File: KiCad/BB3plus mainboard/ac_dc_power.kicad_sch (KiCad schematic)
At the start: 96 parts, among them IC7 SN74HCS02PWR, IC8 TPS62933ODRLR, IC9 LM64460CPPQRYFRQ1, K1 AZ943-1CH-12DE, K2 AZ943-1CH-12DE, Q3 2N7002, Q4 2N7002, Q5 MMBT5401, Q6 DMP3013SFV-7, SW1 WBL2UOAGQR05CLR, X10 B3P-VH-FB-B, X11 B3P-VH-FB-B, X5 571-0400, X6 GSP1.9101.1, X7 1-726388-2, X8 B3P-VH-FB-B, X9 B3P-VH-FB-B

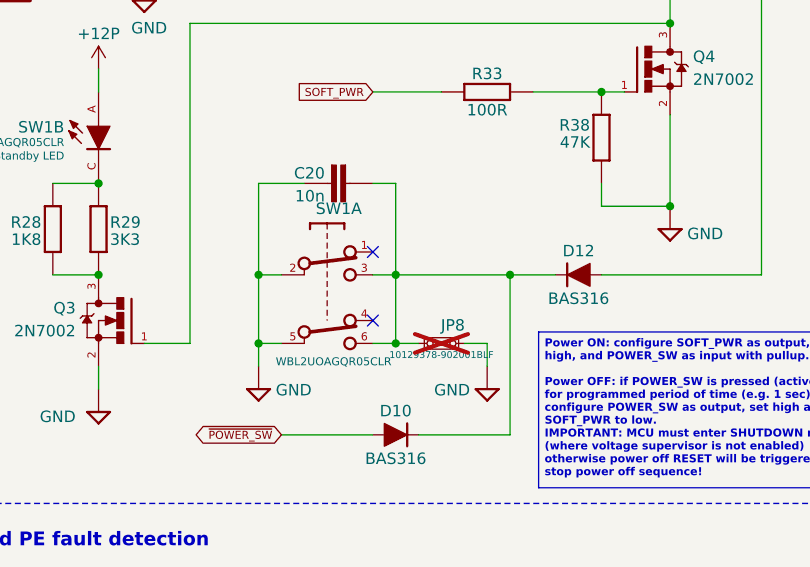
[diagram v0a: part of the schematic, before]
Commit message: JP8 added as mandatory
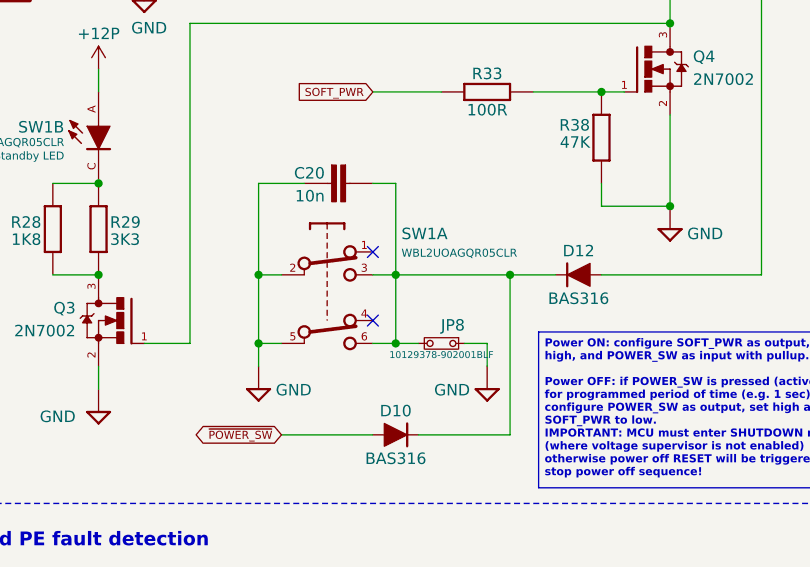
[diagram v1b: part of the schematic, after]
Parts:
- JP8: now fitted; now in the parts list
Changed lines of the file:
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@@
 	(title_block
 		(title "${project_name}")
-		(date "2026-10-05")
+		(date "2026-10-06")
 		(rev "${project_version}")
 		(company "${project_creator}")
@@
 		(dnp no)
 		(property "Reference" "SW1"
-			(at 77.47 117.856 0)
+			(at 86.995 120.65 0)
 			(show_name no)
 			(do_not_autoplace yes)
@@
 		)
 		(property "Value" "WBL2UOAGQR05CLR"
-			(at 73.025 134.62 0)
+			(at 86.995 122.555 0)
 			(show_name no)
 			(do_not_autoplace yes)
@@
 		(body_style 1)
 		(exclude_from_sim no)
-		(in_bom no)
+		(in_bom yes)
 		(on_board yes)
-		(in_pos_files no)
-		(dnp yes)
+		(in_pos_files yes)
+		(dnp no)
 		(property "Reference" "JP8"
 			(at 92.71 130.81 0)

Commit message: #22
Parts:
- renumbered JP8 to JP9
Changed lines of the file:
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@@
 	(title_block
 		(title "${project_name}")
-		(date "2026-10-06")
+		(date "2026-10-08")
 		(rev "${project_version}")
 		(company "${project_creator}")
@@
 		(in_pos_files yes)
 		(dnp no)
-		(property "Reference" "JP8"
-			(at 92.71 130.81 0)
+		(property "Reference" "JP9"
+			(at 91.44 130.81 0)
 			(show_name no)
 			(do_not_autoplace no)
@@
 			(project "BB3plus mainboard"
 				(path "/1df84e4f-233a-4f72-9418-c0020706bb76/451f238c-56e9-49de-804a-2a19deb9fc4a"
-					(reference "JP8")
+					(reference "JP9")
 					(unit 1)
 				)

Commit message: PE fault detection section updated
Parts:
- added C27: 100n, PCM_EEZ_passives:C_0603_1608Metric, symbol PCM_EEZ_passives:C-EU
- added JP10: 10129378-904001BLF, PCM_EEZ_connectors:PinHeader_1x04_P2.54mm_vert_numbered, symbol PCM_EEZ_unsorted:JP4 open 2.54mm THT
- R31, R32: value 33K/0.5W -> 100K/0.5W; footprint PCM_EEZ_passives:R_0805_2012Metric -> PCM_EEZ_passives:R_1210_3225Metric; DigiKey 10-ERJ-P06F3302VCT-ND -> 13-RC2010JK-07100KLCT-ND; LCSC C441988 -> C606205; Mouser 667-ERJ-P06F3302V -> 603-RC2010JK-07100KL; TME ERJP06F3302V -> CQ1210-100K-1%
- ZD3: now not fitted; now left out of the parts list
- renumbered C27 to C28, C28 to C29, C29 to C30, C30 to C31, C31 to C32, C32 to C33, C33 to C34, C34 to C35, C35 to C36, C36 to C37, C37 to C38, C38 to C39, C39 to C40, C40 to C41, C41 to C42, C42 to C43, C43 to C44, C44 to C45, C45 to C46, C46 to C47
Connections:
- net +12V: now also JP10.1
- net +3V3: now also JP10.3
- net +5V: now also JP10.2
- net GND: now also C27.1, JP10.4
- net at IC7.11 (4A), IC7.12 (4B), OK1.4 (COL)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: now also C27.2
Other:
- moved on the sheet: IC7D, R40, TP8

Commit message: Various small changes
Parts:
- added X9: 22-23-2031, Connector_Molex:Molex_KK-254_AE-6410-03A_1x03_P2.54mm_Vertical, symbol Connector_Generic:Conn_01x03
- renumbered C20 to C19, C19 to C20, X9 to X10, X10 to X11, X11 to X12
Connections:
- net GND: now also X9.3 (Pin_3)
- net at C18.1, L1.1, TR1.V+ (+): now also X9.1 (Pin_1)
- no-connect marks 5 -> 6
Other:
- moved on the sheet: C18, C20, L1, TP4, TP5, TP6

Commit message: #24
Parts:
- renumbered C17 to C15, C18 to C16, C19 to C17, C20 to C18, C21 to C19, C22 to C20, C23 to C21, C24 to C22, C25 to C23, C26 to C24, C27 to C25, C28 to C26, C29 to C27, C30 to C28, C31 to C29, C32 to C30, C33 to C31, C34 to C32, C35 to C33, C36 to C34, C37 to C35, C38 to C36, C39 to C37, C40 to C38, C41 to C39, C42 to C40, C43 to C41, C44 to C42, C45 to C43, C46 to C44, C47 to C45, D10 to D4, D11 to D5, D12 to D6, IC7 to IC4, IC8 to IC5, IC9 to IC6, JP9 to JP8, JP10 to JP9, R27 to R24, R28 to R25, R29 to R26, R30 to R27, R31 to R28, R32 to R29, R33 to R30, R34 to R31, R35 to R32, R36 to R33, R37 to R34, R38 to R35, R39 to R36, R40 to R37, R41 to R38, R42 to R39, R43 to R40, R44 to R41, R45 to R42
